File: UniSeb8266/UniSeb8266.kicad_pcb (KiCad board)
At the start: 2 copper layers, 72 x 100 mm, 30 parts, among them IC1 WEMOS-D1-MINI, IC2 GY-BME280-3.3, IC3 LM1117IMPX-, IC4 MCP23008SS, IC5 RT9400, IC6 AMS5915, J1 22-?-0327-2031, X1 AK500/2, X2 AK500/2, X3 233-503, X5 233-504, X61 JST-XH-05-PIN-LONG-PAD, X7 0446200002, X8 233-508

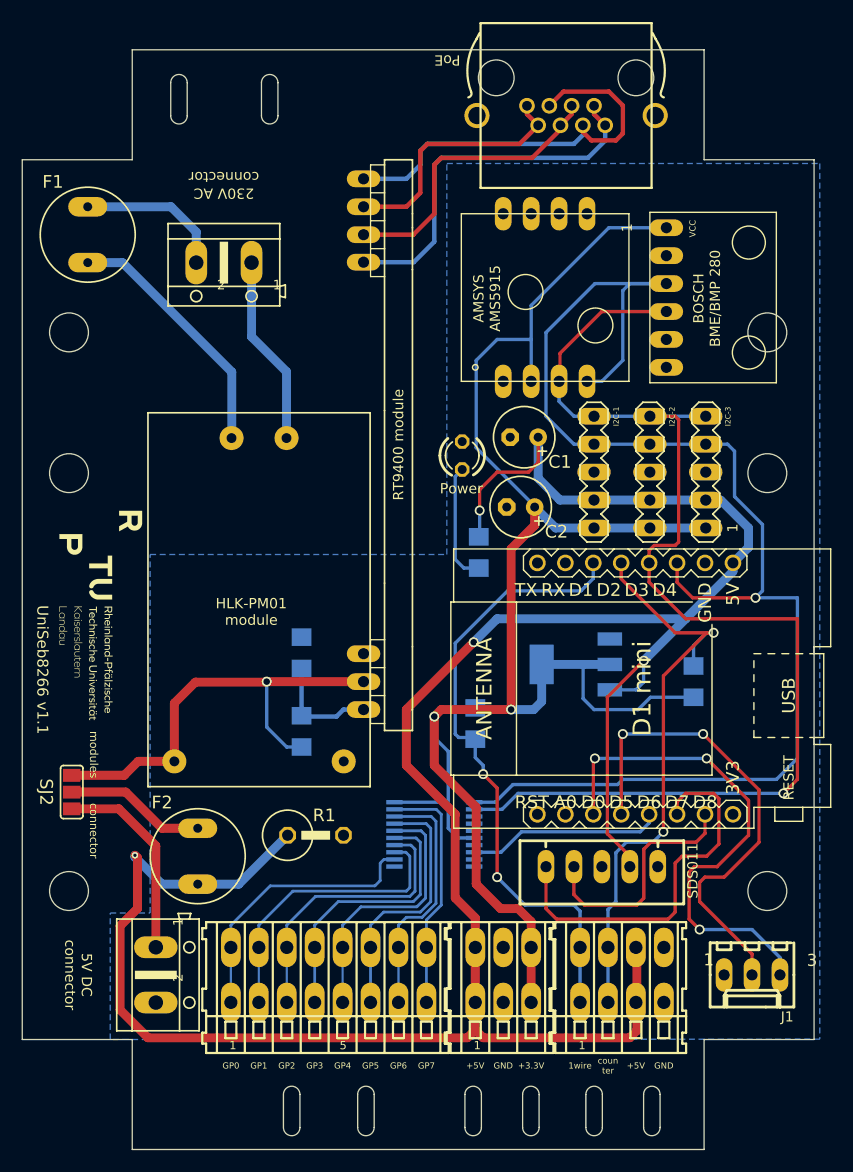
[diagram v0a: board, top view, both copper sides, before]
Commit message: changed name of SJ2 -> SJ1
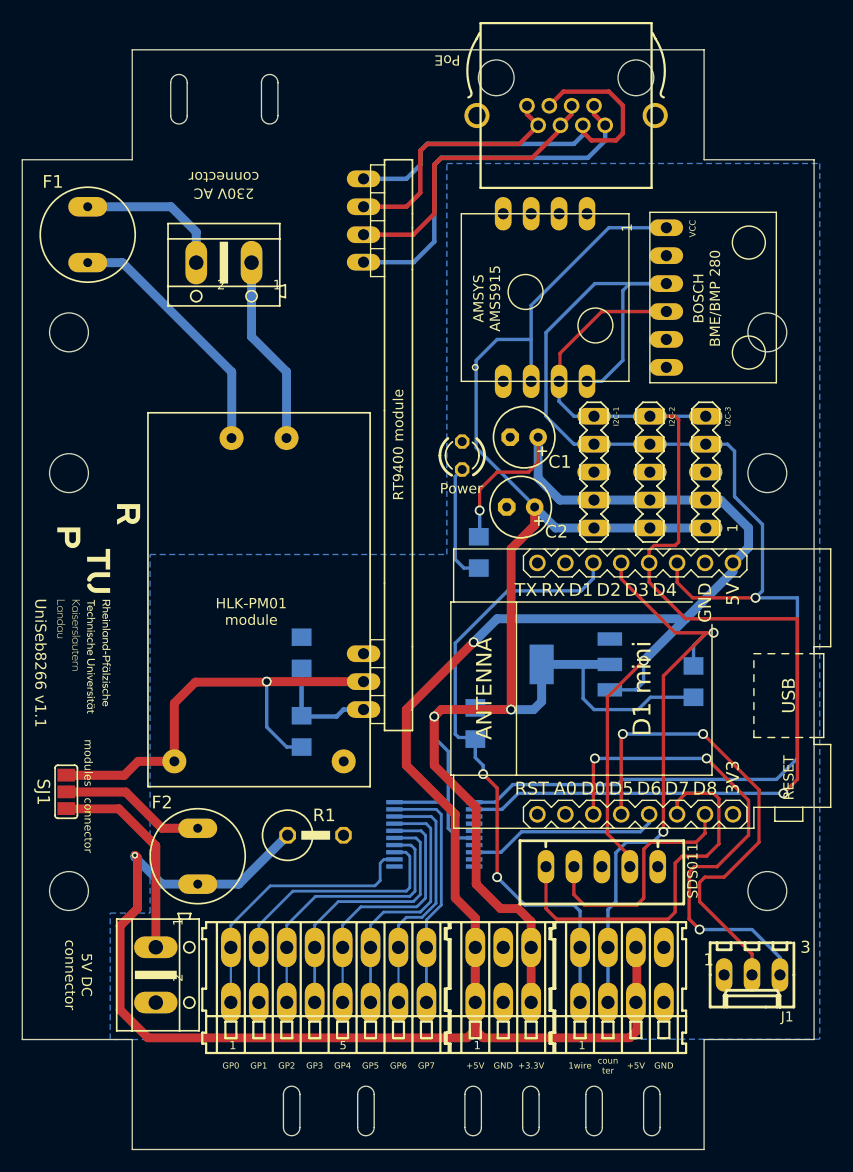
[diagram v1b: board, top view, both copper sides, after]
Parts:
- removed SJ2: SJ2W, UniSeb8266:SJ_2
- added SJ1: SJ2W, UniSeb8266:SJ_2, F.Cu at (116.5, 122.5)
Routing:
- net Net-(X2A-KL): track 18.3 -> 18.8 mm
- net Net-(F2-Pad1): track 12.8 -> 13.3 mm
- net Net-(IC5-+VDC): track 41.5 -> 42.0 mm

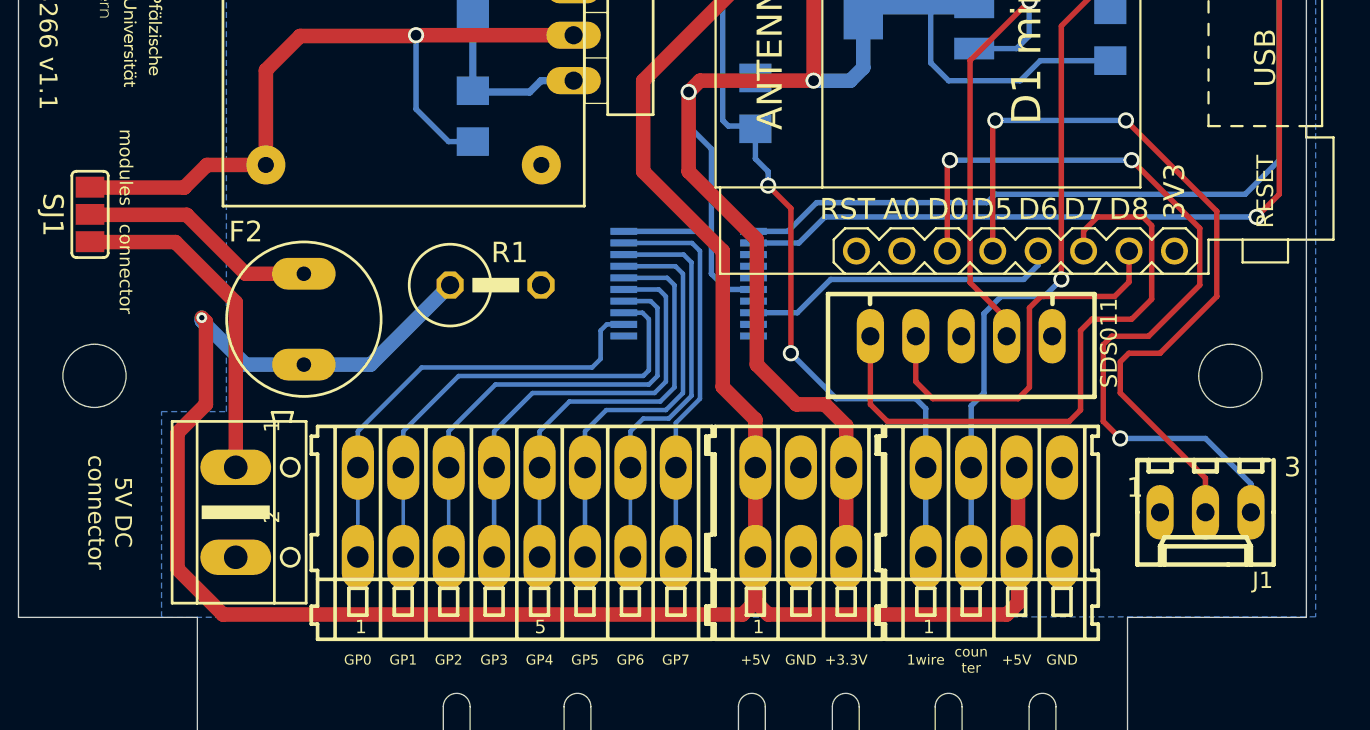
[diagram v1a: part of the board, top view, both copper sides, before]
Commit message: added SJ2 to change pin-2 usage of "Molex KK 254" connector (3.3V or D5)
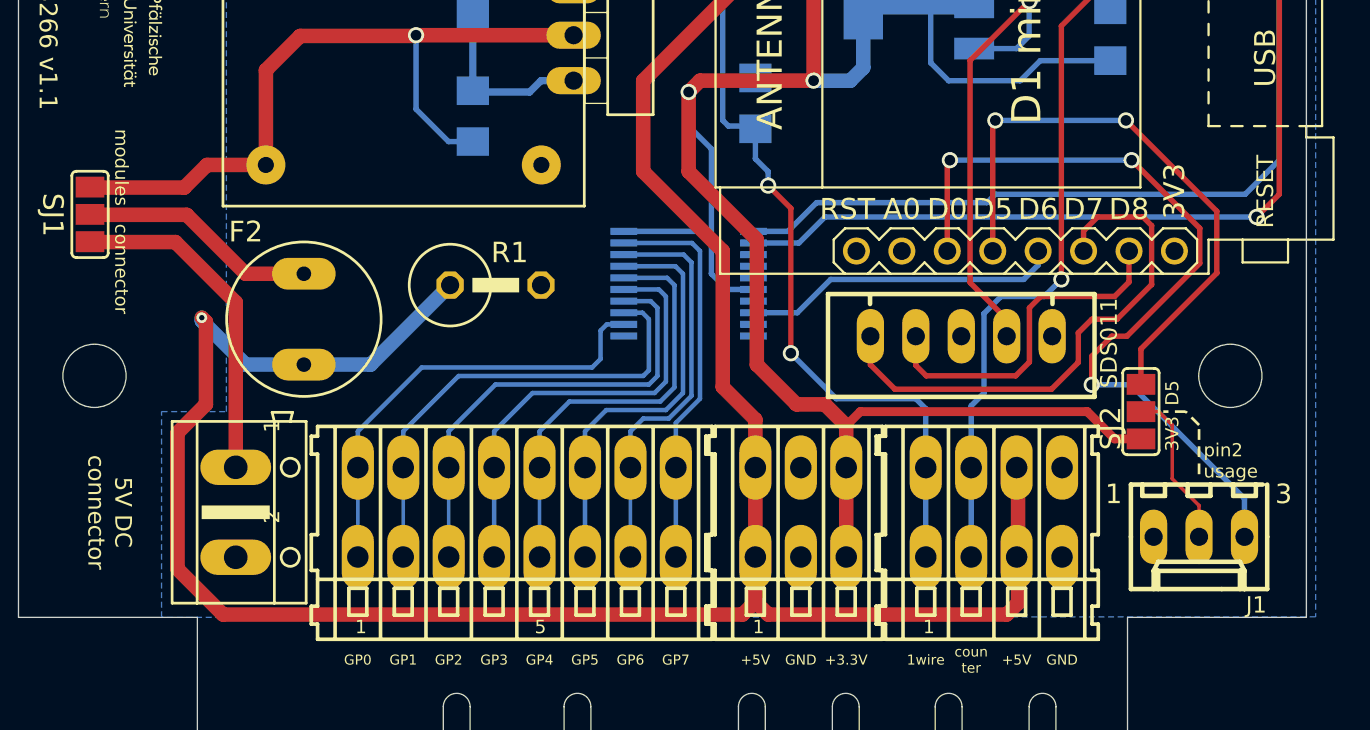
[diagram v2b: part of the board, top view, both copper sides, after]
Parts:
- added SJ2: SJ2W, UniSeb8266:SJ_2, F.Cu at (175.2, 133.5)
- moved J1 1.42 mm to (178.5, 140.5)
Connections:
- J1 pad 2: /D5 -> Net-(J1B-S)
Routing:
- net +3V3: track 165.3 -> 182.7 mm
- net /D5: track 43.9 -> 33.3 mm
- net Net-(J1B-S): track 0.00 -> 8.93 mm
- net /SDS_TX: track 34.9 -> 30.0 mm
- net /SDS_RX: track 21.9 -> 19.5 mm
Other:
- board text added: "3V3"
- board text added: "D5"
- board text added: "pin2 usage"

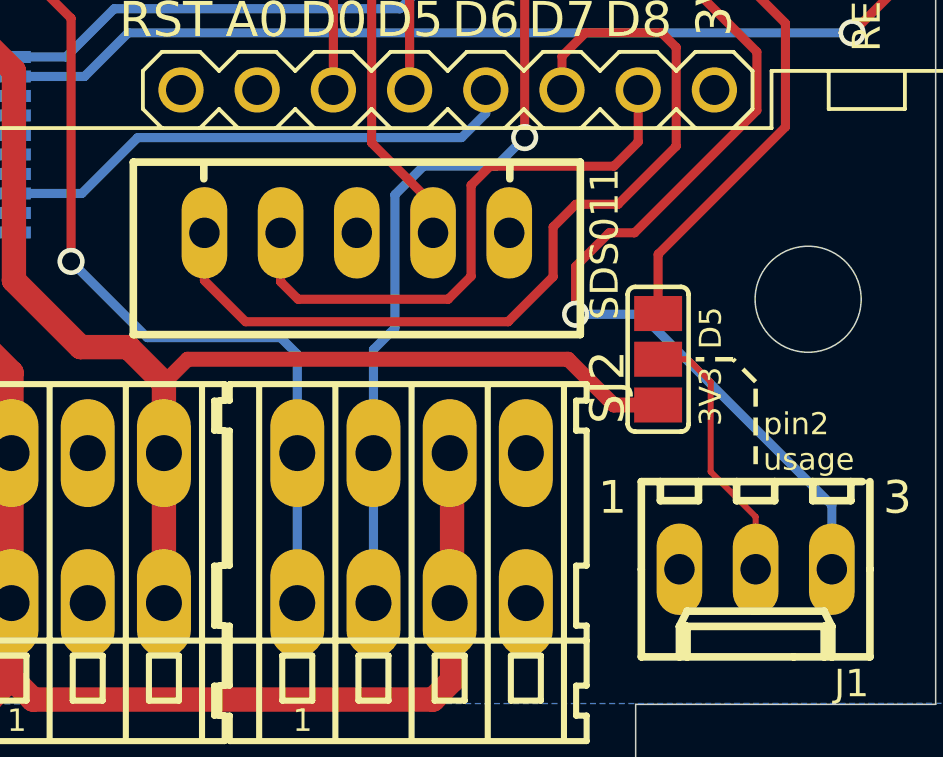
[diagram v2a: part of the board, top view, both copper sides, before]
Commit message: added R2 pullup for pin3 of J1
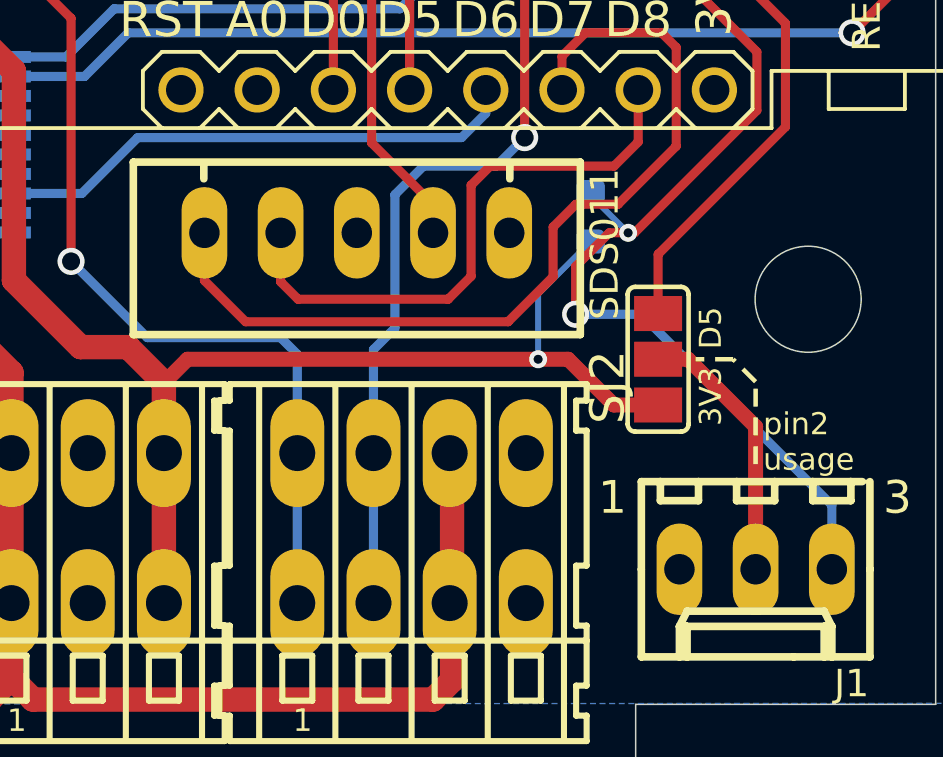
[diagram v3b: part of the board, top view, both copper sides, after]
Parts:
- added R2: 4,7k, Resistor_SMD:R_0603_1608Metric, B.Cu at (173.0, 128.8)
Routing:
- net +3V3: track 182.7 -> 187.4 mm, vias 2 -> 3
- net /D0: track 45.7 -> 47.6 mm, vias 3 -> 4
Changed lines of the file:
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@@
       (net 37 "Net-(IC5-ADJ)") (pinfunction "2") (pintype "passive") (solder_mask_margin 0.0508) (thermal_bridge_angle 0))
   )
+  (footprint "Resistor_SMD:R_0603_1608Metric" (layer "B.Cu")
+    (at 173 128.75 90)
+    (descr "Resistor SMD 0603 (1608 Metric), square (rectangular) end terminal, IPC_7351 nominal, (Body size source: IPC-SM-782 page 72, https://www.pcb-3d.com/wordpress/wp-content/uploads/ipc-sm-782a_amendment_1_and_2.pdf), generated with kicad-footprint-generator")
+    (tags "resistor")
+    (property "LCSC" "C23162")
+    (property "Sheetfile" "UniSeb8266.kicad_sch")
+    (property "Sheetname" "")
+    (attr smd)
+    (fp_text reference "R2" (at 0 1.43 90) (layer "B.SilkS")
+        (effects (font (size 1 1) (thickness 0.15)) (justify mirror))
+    )
+    (fp_text value "4,7k" (at 0 -1.43 90) (layer "B.Fab")
+        (effects (font (size 1 1) (thickness 0.15)) (justify mirror))
+    )
+    (fp_text user "${REFERENCE}" (at 0 0 90) (layer "B.Fab")
+        (effects (font (size 0.4 0.4) (thickness 0.06)) (justify mirror))
+    )
+    (fp_line (start -0.237258 -0.5225) (end 0.237258 -0.5225)
+      (stroke (width 0.12) (type solid)) (layer "B.SilkS"))
+    (fp_line (start -0.237258 0.5225) (end 0.237258 0.5225)
+      (stroke (width 0.12) (type solid)) (layer "B.SilkS"))
+    (fp_line (start -1.48 -0.73) (end -1.48 0.73)
+      (stroke (width 0.05) (type solid)) (layer "B.CrtYd"))
+    (fp_line (start -1.48 0.73) (end 1.48 0.73)
+      (stroke (width 0.05) (type solid)) (layer "B.CrtYd"))
+    (fp_line (start 1.48 -0.73) (end -1.48 -0.73)
+      (stroke (width 0.05) (type solid)) (layer "B.CrtYd"))
+    (fp_line (start 1.48 0.73) (end 1.48 -0.73)
+      (stroke (width 0.05) (type solid)) (layer "B.CrtYd"))
+    (fp_line (start -0.8 -0.4125) (end -0.8 0.4125)
+      (stroke (width 0.1) (type solid)) (layer "B.Fab"))
+    (fp_line (start -0.8 0.4125) (end 0.8 0.4125)
+      (stroke (width 0.1) (type solid)) (layer "B.Fab"))
+    (fp_line (start 0.8 -0.4125) (end -0.8 -0.4125)
+      (stroke (width 0.1) (type solid)) (layer "B.Fab"))
+    (fp_line (start 0.8 0.4125) (end 0.8 -0.4125)
+      (stroke (width 0.1) (type solid)) (layer "B.Fab"))
+    (pad "1" smd roundrect (at -0.825 0 90) (size 0.8 0.95) (layers "B.Cu" "B.Paste" "B.Mask") (roundrect_rratio 0.25)
+      (net 7 "+3V3") (pinfunction "1") (pintype "passive"))
+    (pad "2" smd roundrect (at 0.825 0 90) (size 0.8 0.95) (layers "B.Cu" "B.Paste" "B.Mask") (roundrect_rratio 0.25)
+      (net 16 "/D0") (pinfunction "2") (pintype "passive"))
+    (model "${KICAD6_3DMODEL_DIR}/Resistor_SMD.3dshapes/R_0603_1608Metric.wrl"
+      (offset (xyz 0 0 0))
+      (scale (xyz 1 1 1))
+      (rotate (xyz 0 0 0))
+    )
+  )
   (footprint "UniSeb8266:R1206" (layer "B.Cu")
     (at 173.5411 112.4586 -90)
@@
   (segment (start 156.9511 100.3936) (end 156.9511 114.9986) (width 0.8128) (layer "F.Cu") (net 7))
   (segment (start 158.7761 134.2861) (end 158.7761 136.6286) (width 0.8128) (layer "F.Cu") (net 7))
+  (segment (start 171.25 133.5) (end 159.5622 133.5) (width 0.5) (layer "F.Cu") (net 7))
   (segment (start 150.6011 114.9986) (end 156.9511 114.9986) (width 0.8128) (layer "F.Cu") (net 7))
   (segment (start 153.7761 130.8736) (end 153.7761 123.8886) (width 0.8128) (layer "F.Cu") (net 7))
   (segment (start 153.7761 123.8886) (end 149.9661 120.0786) (width 0.8128) (layer "F.Cu") (net 7))
   (segment (start 175.25 135.024) (end 173.774 135.024) (width 0.5) (layer "F.Cu") (net 7))
+  (segment (start 172.25 133.5) (end 171.25 133.5) (width 0.5) (layer "F.Cu") (net 7))
   (segment (start 156.9511 100.3936) (end 159.0936 98.2511) (width 0.8128) (layer "F.Cu") (net 7))
   (segment (start 155.9986 133.0961) (end 153.7761 130.8736) (width 0.8128) (layer "F.Cu") (net 7))
@@
   (segment (start 159.0936 96.5836) (end 159.0936 98.2511) (width 0.8128) (layer "F.Cu") (net 7))
   (segment (start 159.5622 133.5) (end 158.7761 134.2861) (width 0.5) (layer "F.Cu") (net 7))
-  (segment (start 172.25 133.5) (end 159.5622 133.5) (width 0.5) (layer "F.Cu") (net 7))
   (segment (start 149.9661 120.0786) (end 149.9661 115.6336) (width 0.8128) (layer "F.Cu") (net 7))
   (segment (start 158.7761 136.6286) (end 158.7761 141.6286) (width 0.8128) (layer "F.Cu") (net 7))
   (via (at 156.9511 114.9986) (size 0.9048) (drill 0.6) (layers "F.Cu" "B.Cu") (net 7))
+  (via (at 171.25 133.5) (size 0.6) (drill 0.3) (layers "F.Cu" "B.Cu") (net 7))
   (via (at 149.9661 115.6336) (size 0.9048) (drill 0.6) (layers "F.Cu" "B.Cu") (net 7))
   (segment (start 151.0886 123.4236) (end 151.2361 123.5711) (width 0.3048) (layer "B.Cu") (net 7))
@@
   (segment (start 159.7291 110.8948) (end 159.7291 114.2756) (width 0.8128) (layer "B.Cu") (net 7))
   (segment (start 155.6811 81.3436) (end 158.7761 81.3436) (width 0.3048) (layer "B.Cu") (net 7))
+  (segment (start 173 129.575) (end 171.25 131.325) (width 0.2) (layer "B.Cu") (net 7))
   (segment (start 158.7761 81.3436) (end 158.7761 78.2486) (width 0.3048) (layer "B.Cu") (net 7))
   (segment (start 168.5011 115.0036) (end 164.5011 115.0036) (width 0.3048) (layer "B.Cu") (net 7))
@@
   (segment (start 151.2361 125.7936) (end 152.1161 126.6736) (width 0.3048) (layer "B.Cu") (net 7))
   (segment (start 160.9986 98.4886) (end 159.0936 96.5836) (width 0.8128) (layer "B.Cu") (net 7))
+  (segment (start 171.25 131.325) (end 171.25 133.5) (width 0.2) (layer "B.Cu") (net 7))
   (segment (start 151.2361 118.8086) (end 149.9661 117.5386) (width 0.3048) (layer "B.Cu") (net 7))
   (segment (start 153.7761 83.2486) (end 155.6811 81.3436) (width 0.3048) (layer "B.Cu") (net 7))
@@
   (segment (start 178.5411 125.2089) (end 178.5411 123.2536) (width 0.3048) (layer "F.Cu") (net 16))
   (segment (start 172.5 130.40595) (end 173.61985 129.2861) (width 0.3048) (layer "F.Cu") (net 16))
-  (segment (start 173.61985 129.2861) (end 174.4639 129.2861) (width 0.3048) (layer "F.Cu") (net 16))
+  (segment (start 173.61985 129.2861) (end 174.25 129.2861) (width 0.3048) (layer "F.Cu") (net 16))
   (segment (start 178.5411 123.2536) (end 174.7311 119.4436) (width 0.3048) (layer "F.Cu") (net 16))
+  (segment (start 174.25 129.2861) (end 174.4639 129.2861) (width 0.3048) (layer "F.Cu") (net 16))
   (segment (start 164.4251 119.6151) (end 164.5711 119.4436) (width 0.3048) (layer "F.Cu") (net 16))
   (via (at 172.5 132) (size 0.9048) (drill 0.6) (layers "F.Cu" "B.Cu") (net 16))
+  (via (at 174.25 129.2861) (size 0.6) (drill 0.3) (layers "F.Cu" "B.Cu") (net 16))
   (via (at 164.5711 119.4436) (size 0.9048) (drill 0.6) (layers "F.Cu" "B.Cu") (net 16))
   (via (at 174.7311 119.4436) (size 0.9048) (drill 0.6) (layers "F.Cu" "B.Cu") (net 16))
@@
   (segment (start 172.5 132) (end 174.67875 132) (width 0.3048) (layer "B.Cu") (net 16))
   (segment (start 174.7311 119.4436) (end 164.5711 119.4436) (width 0.3048) (layer "B.Cu") (net 16))
+  (segment (start 173 127.925) (end 173 128.0361) (width 0.2) (layer "B.Cu") (net 16))
+  (segment (start 173 128.0361) (end 174.25 129.2861) (width 0.2) (layer "B.Cu") (net 16))
   (segment (start 179.4936 125.7564) (end 175.25 130) (width 0.3048) (layer "F.Cu") (net 17))
   (segment (start 175.25 130) (end 175.25 131.976) (width 0.3048) (layer "F.Cu") (net 17))
@@
   (segment (start 133.3507 81.1007) (end 136.5311 84.2811) (width 0.8128) (layer "B.Cu") (net 44))
   (segment (start 133.3507 74.3586) (end 133.3507 81.1007) (width 0.8128) (layer "B.Cu") (net 44))
-  (segment (start 177 134.25) (end 177 137.25) (width 0.2) (layer "F.Cu") (net 48))
-  (segment (start 175.25 133.5) (end 176.25 133.5) (width 0.2) (layer "F.Cu") (net 48))
-  (segment (start 176.25 133.5) (end 177 134.25) (width 0.2) (layer "F.Cu") (net 48))
-  (segment (start 177 137.25) (end 178.5 138.75) (width 0.2) (layer "F.Cu") (net 48))
-  (segment (start 178.5 138.75) (end 178.5 140.5) (width 0.2) (layer "F.Cu") (net 48))
+  (segment (start 175.25 133.5) (end 176.25 133.5) (width 0.5) (layer "F.Cu") (net 48))
+  (segment (start 176.25 133.5) (end 178.5 135.75) (width 0.5) (layer "F.Cu") (net 48))
+  (segment (start 178.5 135.75) (end 178.5 140.5) (width 0.5) (layer "F.Cu") (net 48))
   (zone (net 1) (net_name "GND") (layer "B.Cu") (hatch edge 0.5)
     (priority 6)
